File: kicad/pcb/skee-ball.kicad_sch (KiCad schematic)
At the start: 53 parts, among them J1 SPEAKER_P, J10 NHD_RW, J11 NHD_DB1, J12 NHD_DB0, J13 US_ECHO0, J14 US_ECHO1, J15 US_ECHO2, J16 US_ECHO3, J17 US_ECHO4, J18 US_TRIG0_5, J19 US_TRIG1_5, J2 SPEAKER_N, J20 US_TRIG2_5, J21 US_TRIG3_5, J22 US_TRIG4_5, J23 NHD_E2, J24 NHD_E2, J25 ADC_IN1, J26 PWM_SERVO_6, J27 PWM_DC (TIM17_CH1), J28 BUTTON, J29 NHD_V0, J3 NHD_DB7, J4 NHD_DB6, J5 NHD_DB5, J6 NHD_DB4, J7 NHD_DB3, J8 NHD_DB2, J9 NHD_RS, U1 D24V22F6, U10 LD1117S33TR_SOT223, U11 LD1117S33TR_SOT223, U12 LD1117S33TR_SOT223, U13 LD1117S33TR_SOT223, U14 LD1117S33TR_SOT223, U2 MAX98357A, U3 D24V22F5, U4 STM32F091RCTx, U5 74HC595, U6 74HC595, U7 74LS08, U8 LD1117S33TR_SOT223, U9 LD1117S33TR_SOT223

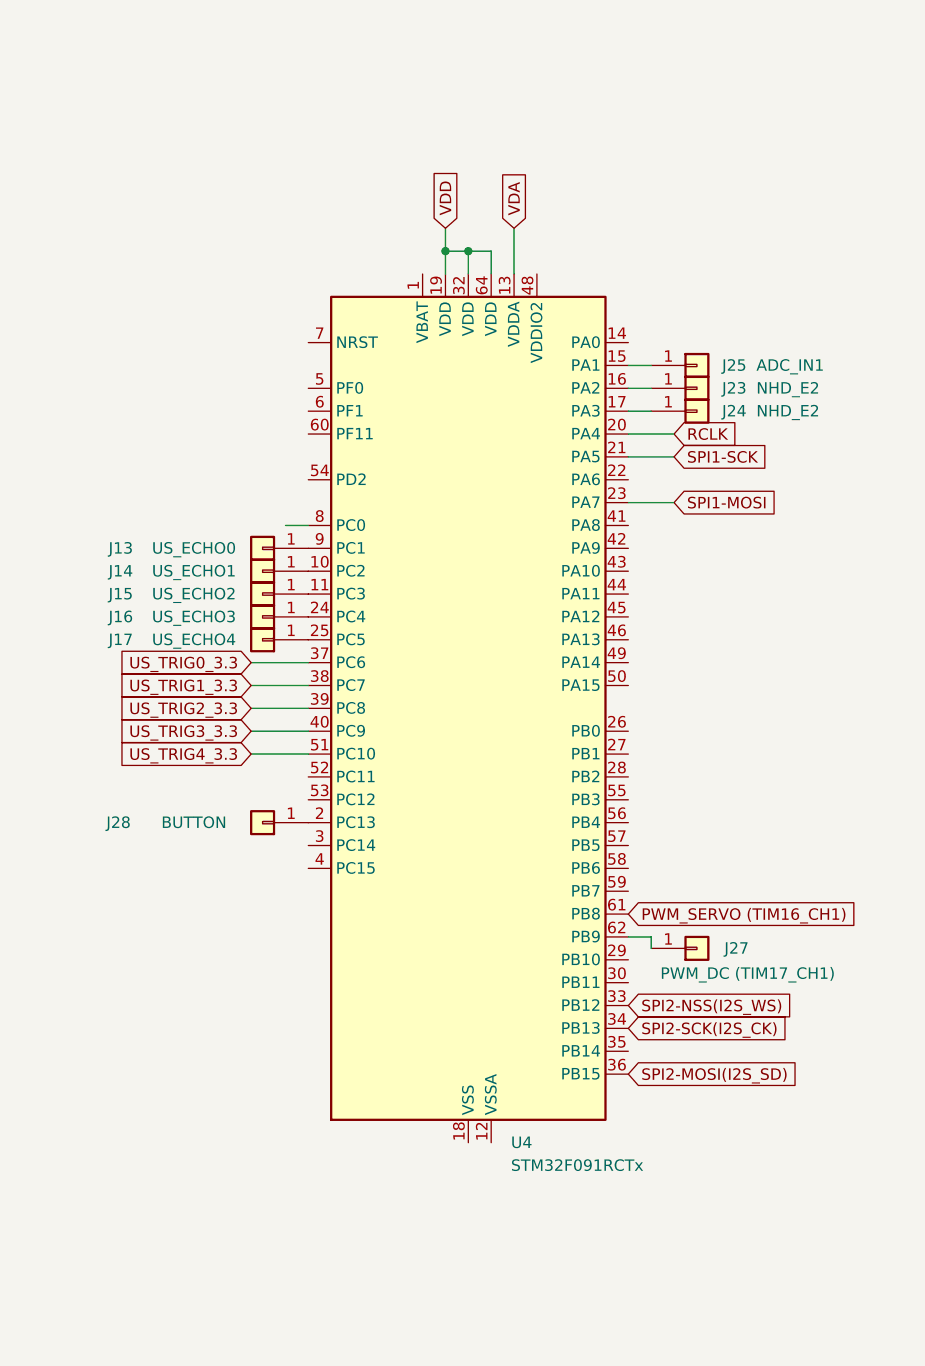
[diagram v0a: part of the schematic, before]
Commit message: added header connection pins
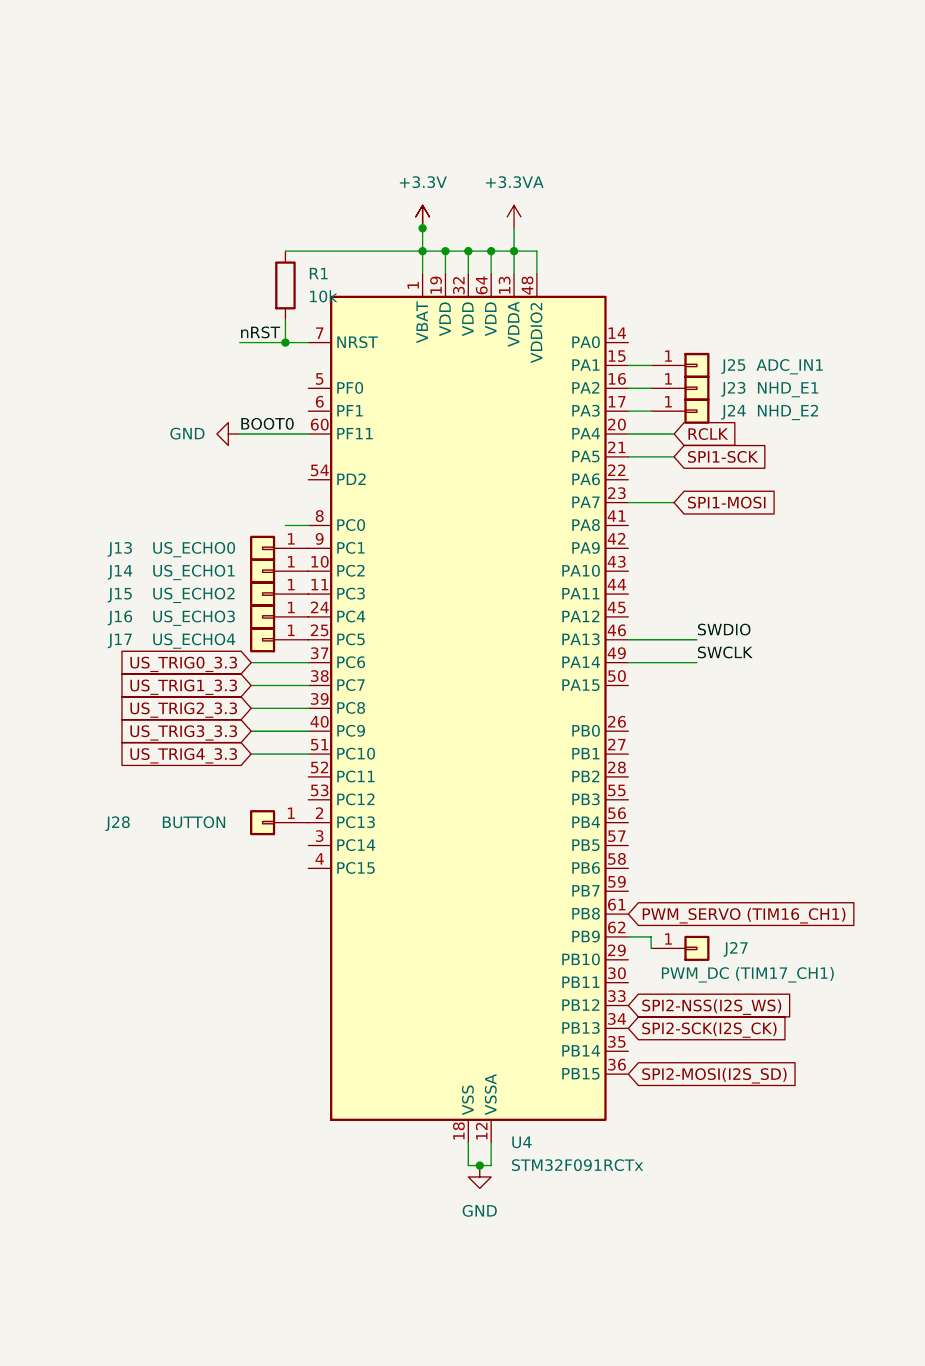
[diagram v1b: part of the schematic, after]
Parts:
- added R1: 10k, symbol Device:R
- J23: value NHD_E2 -> NHD_E1
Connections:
- net +3.3V: now also U4.1 (VBAT), U4.48 (VDDIO2), R1.1
- net GND: now also U4.12 (VSSA), U4.18 (VSS), U4.31 (VSS), U4.47 (VSS), U4.60 (PF11), U4.63 (VSS)
- net SWDIO: now reaches U4.46 (PA13)
- net SWCLK: now reaches U4.49 (PA14)
- net nRST: now reaches U4.7 (NRST)
- net nRST: now also R1.2

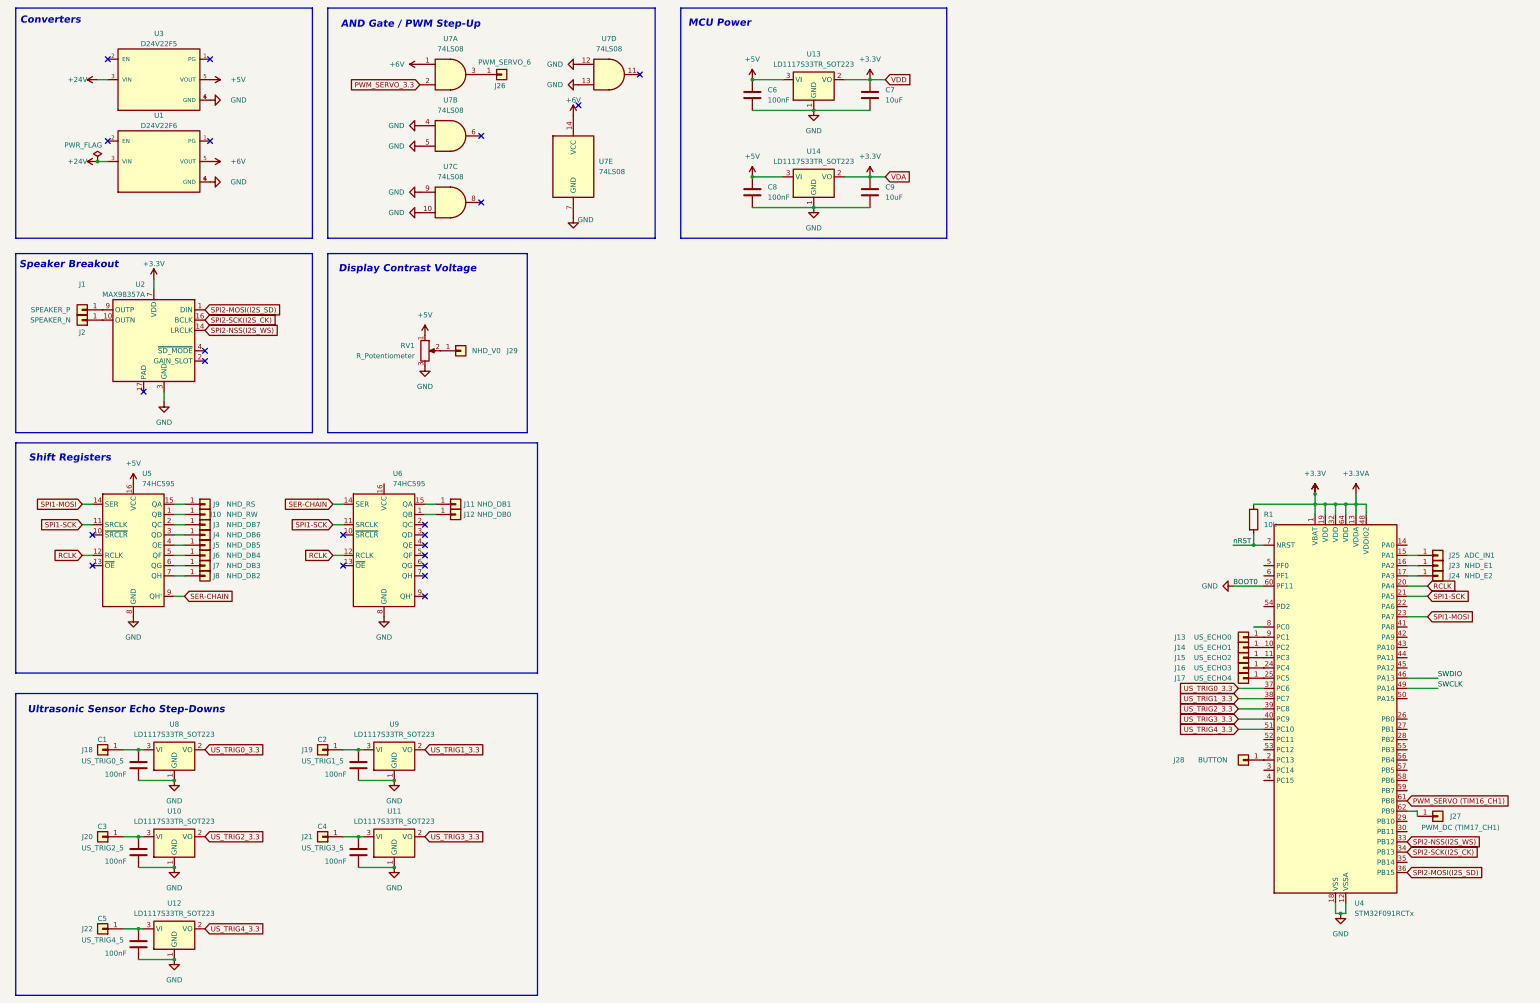
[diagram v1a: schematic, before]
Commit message: add debugging circuitry to schematic
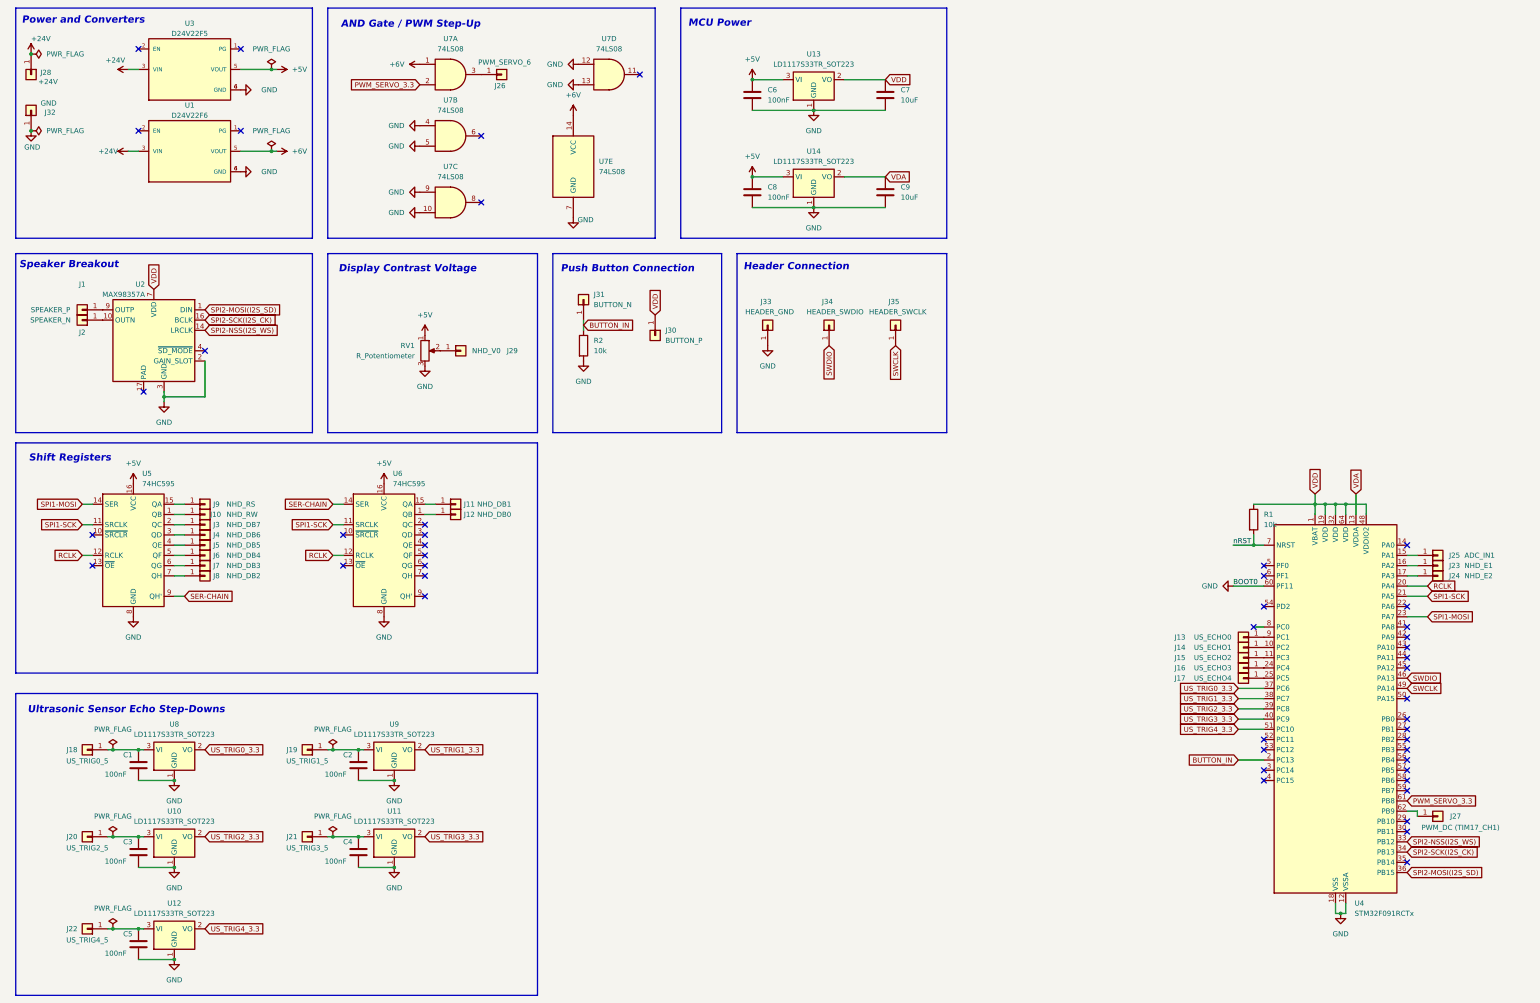
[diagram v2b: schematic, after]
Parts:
- added J30: BUTTON_P, symbol Connector_Generic:Conn_01x01
- added J31: BUTTON_N, symbol Connector_Generic:Conn_01x01
- added J32: GND, symbol Connector_Generic:Conn_01x01
- added J33: HEADER_GND, symbol Connector_Generic:Conn_01x01
- added J34: HEADER_SWDIO, symbol Connector_Generic:Conn_01x01
- added J35: HEADER_SWCLK, symbol Connector_Generic:Conn_01x01
- added R2: 10k, symbol Device:R
- J28: value BUTTON -> +24V
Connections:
- net PWM_SERVO (TIM16_CH1) is gone; now on net PWM_SERVO_3.3: U4.61 (PB8)
- net +24V: now also J28.1 (Pin_1)
- net +5V: now also U6.16 (VCC)
- net GND: now also U2.2 (GAIN_SLOT), J32.1 (Pin_1), J33.1 (Pin_1), R2.2
- net SWCLK: now also J35.1 (Pin_1)
- net SWDIO: now also J34.1 (Pin_1)
- net BUTTON_IN: now reaches U4.2 (PC13)
- net BUTTON_IN: now also J31.1 (Pin_1), R2.1; no longer J28.1 (Pin_1)
- net +3.3V renamed VDD
- net VDD: now also J30.1 (Pin_1); no longer C9.1, U14.2 (VO), U4.13 (VDDA)
- new net VDA: C9.1, U14.2 (VO), U4.13 (VDDA)
- no-connect marks 22 -> 47
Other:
- note added: "Header Connection"
- note added: "Power and Converters"
- note added: "Push Button Connection"
- note removed: "Converters"
- moved on the sheet: C7, C9, J18, J19, J20, J21, J22, U1, U3

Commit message: add debugging circuitry to schematic
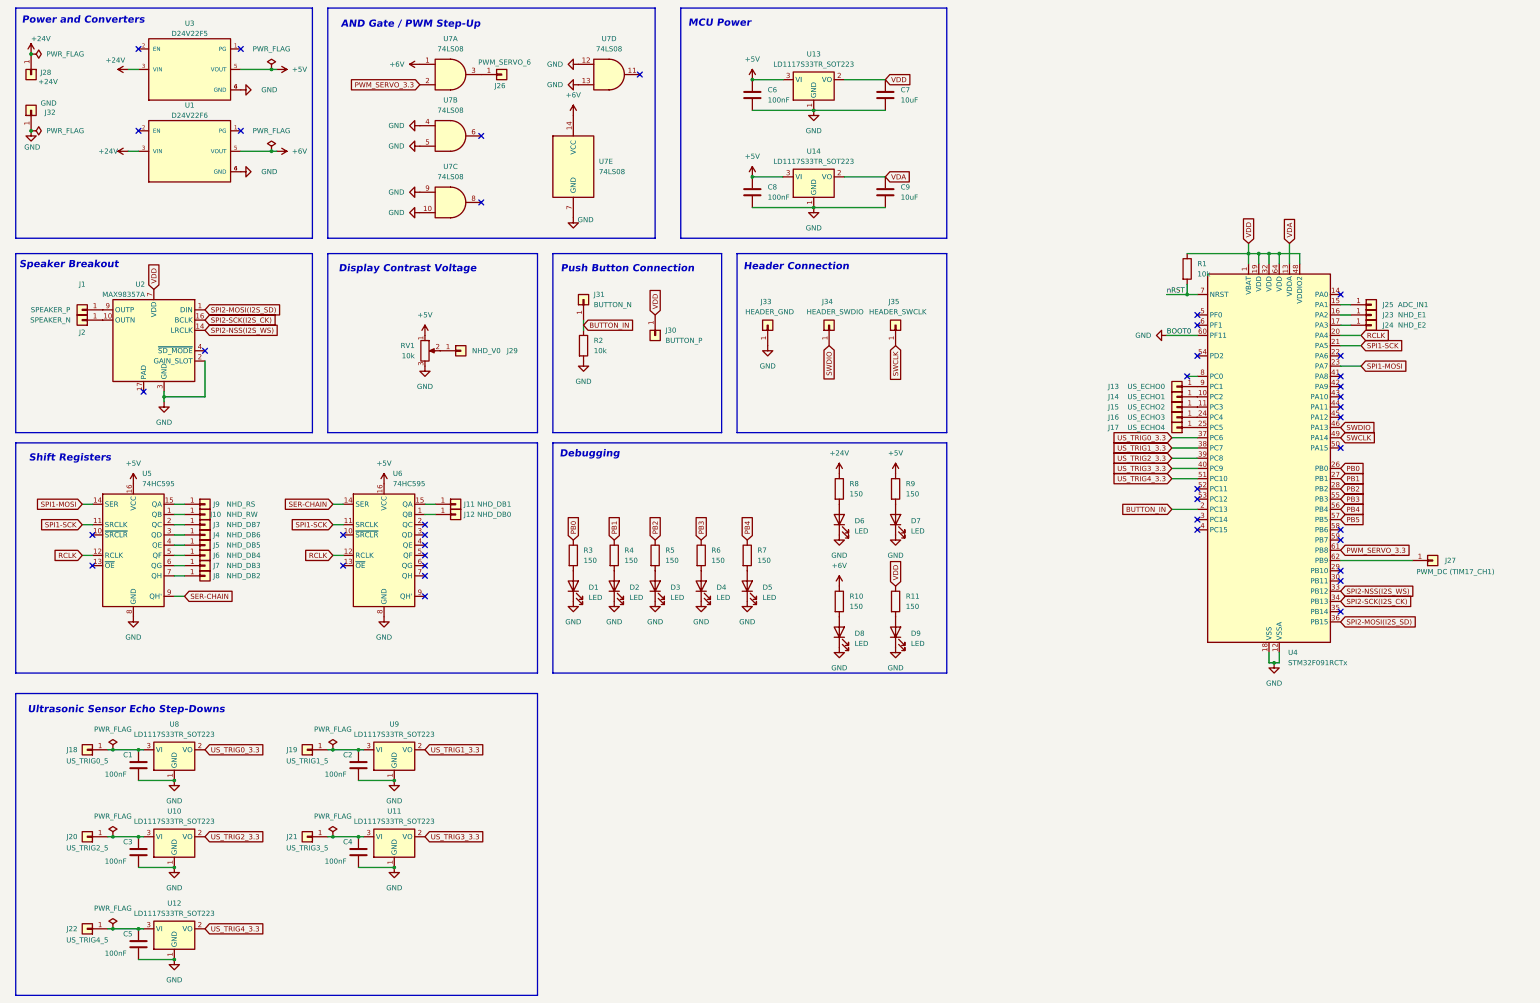
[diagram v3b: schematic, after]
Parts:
- added D1, D2, D3, D4, D5, D6, D7, D8, D9: LED, symbol Device:LED
- added R10, R11, R3, R4, R5, R6, R7, R8, R9: 150, symbol Device:R
- RV1: value R_Potentiometer -> 10k
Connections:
- net +24V: now also R8.1
- net +5V: now also R9.1
- net +6V: now also R10.1
- net GND: now also D1.1 (K), D2.1 (K), D3.1 (K), D4.1 (K), D5.1 (K), D6.1 (K), D7.1 (K), D8.1 (K), D9.1 (K)
- net VDD: now also R11.1
- net PB0: now reaches U4.26 (PB0)
- net PB0: now also R3.1
- net PB1: now reaches U4.27 (PB1)
- net PB1: now also R4.1
- net PB2: now reaches U4.28 (PB2)
- net PB2: now also R5.1
- net PB3: now reaches U4.55 (PB3)
- net PB3: now also R6.1
- net PB4: now reaches U4.56 (PB4)
- net PB4: now also R7.1
- net PB5: now reaches U4.57 (PB5)
- new net: D6.2 (A), R8.2
- new net: D9.2 (A), R11.2
- new net: D8.2 (A), R10.2
- new net: D3.2 (A), R5.2
- new net: D2.2 (A), R4.2
- new net: D4.2 (A), R6.2
- new net: D7.2 (A), R9.2
- new net: D5.2 (A), R7.2
- new net: D1.2 (A), R3.2
- no-connect marks 47 -> 41
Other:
- note added: "Debugging"
- moved on the sheet: J13, J14, J15, J16, J17, J23, J24, J25, J27, R1, U4
